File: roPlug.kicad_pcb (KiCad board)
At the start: 2 copper layers, 25 x 25 mm, 18 parts, among them P1 USB_C_Plug, SW1 Rotary_Encoder_Switch, U1 ATmega32U4-MU, Y1 16MHz

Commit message: change edgemount usb plug to sidemount due to supply issues with pcba
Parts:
- P1: footprint misc:GCT_USB4155-03-C_REVA -> Connector_USB:USB_C_Plug_Molex_105444
- RST1: footprint Connector_PinHeader_2.54mm:PinHeader_1x01_P2.54mm_Vertical -> Connector_PinSocket_2.54mm:PinSocket_1x01_P2.54mm_Vertical
- Y1: footprint Crystal:Crystal_SMD_0603-4Pin_6.0x3.5mm -> Crystal:Crystal_SMD_Abracon_ABM3B-4Pin_5.0x3.2mm
- moved P1 1.30 mm to (112.5, 75.0), turned to 180 degrees
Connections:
- P1 pad S1: (no net) -> Net-(P1-PadS1)
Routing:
- net GND: track 42.6 -> 47.7 mm, vias 8 -> 7
- net Net-(F1-Pad2): track 17.2 -> 20.2 mm
- net D-: track 24.2 -> 26.9 mm
- net D+: track 24.3 -> 27.0 mm
- net Net-(P1-PadB5): track 9.82 -> 10.2 mm, vias 2 -> 1
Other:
- board size 25 x 25 mm -> 25 x 26 mm

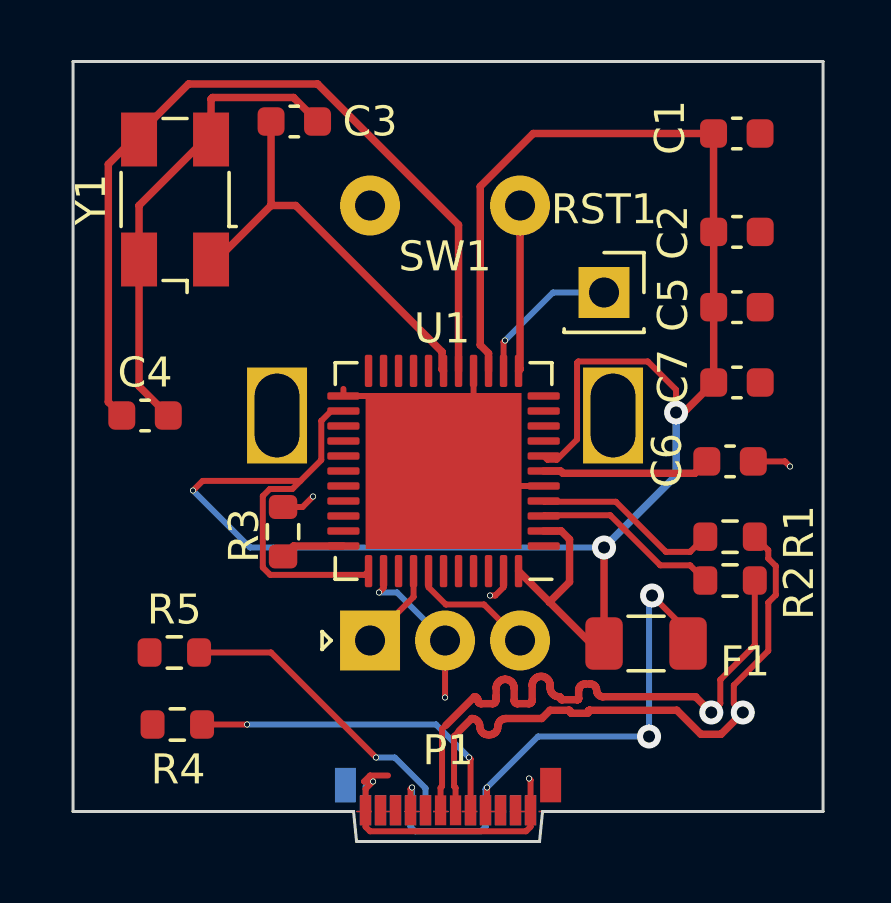
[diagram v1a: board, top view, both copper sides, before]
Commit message: connect the unconnected ground pins on the usb plug
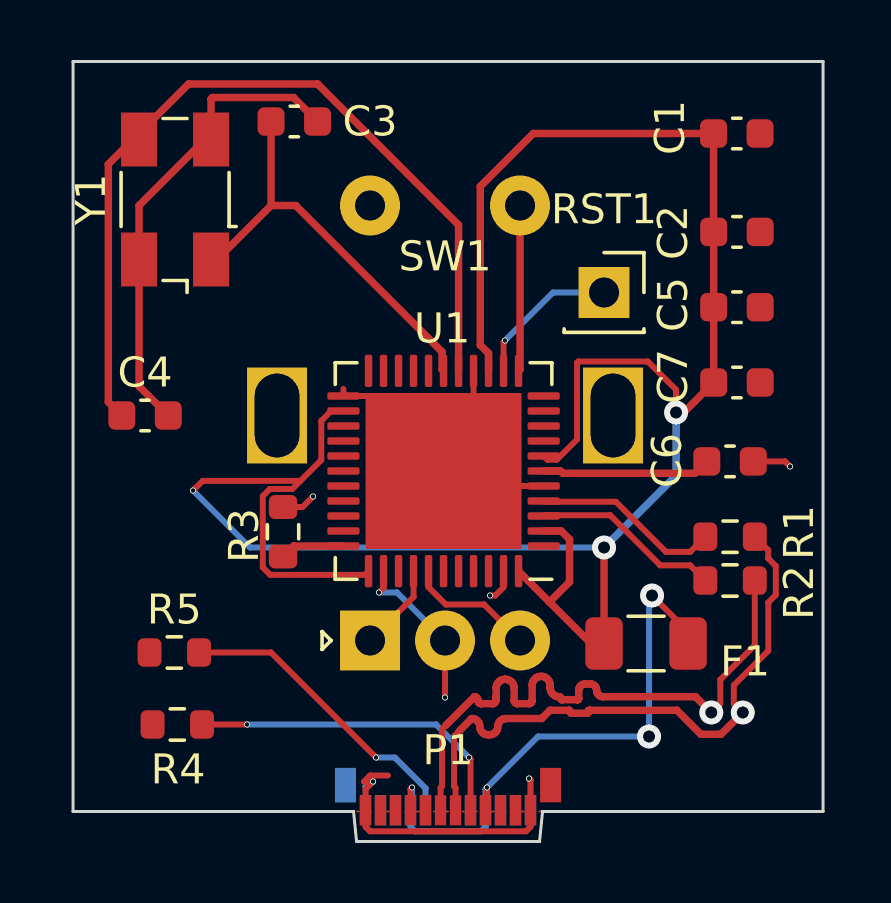
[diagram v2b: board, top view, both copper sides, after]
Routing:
- net GND: track 47.7 -> 49.1 mm
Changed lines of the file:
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@@
     (thickness 0.8)
     (drawings 9)
-    (tracks 384)
+    (tracks 388)
     (zones 0)
     (modules 18)
@@
   (page A4)
   (layers
-    (0 F.Cu signal)
+    (0 F.Cu signal hide)
     (31 B.Cu signal)
     (32 B.Adhes user)
-    (33 F.Adhes user)
+    (33 F.Adhes user hide)
     (34 B.Paste user)
-    (35 F.Paste user)
+    (35 F.Paste user hide)
     (36 B.SilkS user)
     (37 F.SilkS user)
     (38 B.Mask user)
-    (39 F.Mask user)
+    (39 F.Mask user hide)
     (40 Dwgs.User user)
     (41 Cmts.User user hide)
@@
       (effects (font (size 1 1) (thickness 0.15)))
     )
-    (fp_text user %R (at 0 0 90) (layer F.Fab)
-      (effects (font (size 1 1) (thickness 0.15)))
-    )
     (fp_line (start -2.3 -1.6) (end 2.3 -1.6) (layer F.Fab) (width 0.1))
     (fp_line (start 2.3 -1.6) (end 2.5 -1.4) (layer F.Fab) (width 0.1))
@@
     (fp_circle (center 0 0) (end 0.266667 0) (layer F.Adhes) (width 0.166667))
     (fp_circle (center 0 0) (end 0.116667 0) (layer F.Adhes) (width 0.233333))
+    (fp_text user %R (at 0 0 90) (layer F.Fab)
+      (effects (font (size 1 1) (thickness 0.15)))
+    )
     (pad 4 smd rect (at -2 -1.2 90) (size 1.8 1.2) (layers F.Cu F.Paste F.Mask)
       (net 1 GND))
@@
     )
     (fp_text value Conn_01x01_Female (at 0 2.77) (layer F.Fab)
-      (effects (font (size 1 1) (thickness 0.15)))
-    )
-    (fp_text user %R (at 0 0) (layer F.Fab)
       (effects (font (size 1 1) (thickness 0.15)))
     )
@@
     (fp_line (start 1.75 1.75) (end -1.8 1.75) (layer F.CrtYd) (width 0.05))
     (fp_line (start -1.8 1.75) (end -1.8 -1.8) (layer F.CrtYd) (width 0.05))
+    (fp_text user %R (at 0 0) (layer F.Fab)
+      (effects (font (size 1 1) (thickness 0.15)))
+    )
     (pad 1 thru_hole rect (at 0 0) (size 1.7 1.7) (drill 1) (layers *.Cu *.Mask)
       (net 15 "Net-(RST1-Pad1)"))
@@
       (effects (font (size 1 1) (thickness 0.15)))
     )
-    (fp_text user %R (at 11.1 6.3 90) (layer F.Fab)
-      (effects (font (size 1 1) (thickness 0.15)))
-    )
     (fp_line (start 4.5 2.5) (end 10.5 2.5) (layer F.Fab) (width 0.12))
     (fp_line (start 7.5 -0.5) (end 7.5 5.5) (layer F.Fab) (width 0.12))
@@
     (fp_line (start 16 9.6) (end -1.5 9.6) (layer F.CrtYd) (width 0.05))
     (fp_circle (center 7.5 2.5) (end 10.5 2.5) (layer F.Fab) (width 0.12))
+    (fp_text user %R (at 11.1 6.3 90) (layer F.Fab)
+      (effects (font (size 1 1) (thickness 0.15)))
+    )
     (pad S1 thru_hole circle (at 14.5 5 90) (size 2 2) (drill 1) (layers *.Cu *.Mask)
       (net 12 "Net-(SW1-PadS1)"))
@@
     )
     (fp_text value ATmega32U4-MU (at 0 4.82) (layer F.Fab)
-      (effects (font (size 1 1) (thickness 0.15)))
-    )
-    (fp_text user %R (at 0 0) (layer F.Fab)
       (effects (font (size 1 1) (thickness 0.15)))
     )
@@
     (fp_line (start 3.61 -3.61) (end 3.61 -2.885) (layer F.SilkS) (width 0.12))
     (fp_line (start 2.885 -3.61) (end 3.61 -3.61) (layer F.SilkS) (width 0.12))
+    (fp_text user %R (at 0 0) (layer F.Fab)
+      (effects (font (size 1 1) (thickness 0.15)))
+    )
     (pad 1 smd roundrect (at -3.3375 -2.5 180) (size 1.075 0.25) (layers F.Cu F.Paste F.Mask) (roundrect_rratio 0.25))
     (pad 2 smd roundrect (at -3.3375 -2 180) (size 1.075 0.25) (layers F.Cu F.Paste F.Mask) (roundrect_rratio 0.25)
@@
   (segment (start 109.75 75.510002) (end 109.899999 75.660001) (width 0.2) (layer F.Cu) (net 1))
   (segment (start 109.75 74.96) (end 109.75 75.510002) (width 0.2) (layer F.Cu) (net 1))
+  (segment (start 109.85 74.15) (end 110 74) (width 0.2) (layer B.Cu) (net 1))
+  (segment (start 109.75 74.15) (end 109.85 74.15) (width 0.2) (layer B.Cu) (net 1))
+  (segment (start 115.25 73.95) (end 115.2 73.9) (width 0.2) (layer B.Cu) (net 1))
+  (segment (start 115.25 74.96) (end 115.25 73.95) (width 0.2) (layer B.Cu) (net 1))
   (segment (start 121.35 55.675) (end 121.355 55.68) (width 0.25) (layer F.Cu) (net 2))
   (segment (start 121.35 52.4) (end 121.35 55.675) (width 0.25) (layer F.Cu) (net 2))
